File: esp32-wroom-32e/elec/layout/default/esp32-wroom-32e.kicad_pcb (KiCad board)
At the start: 2 copper layers, 40 x 40 mm, 16 parts

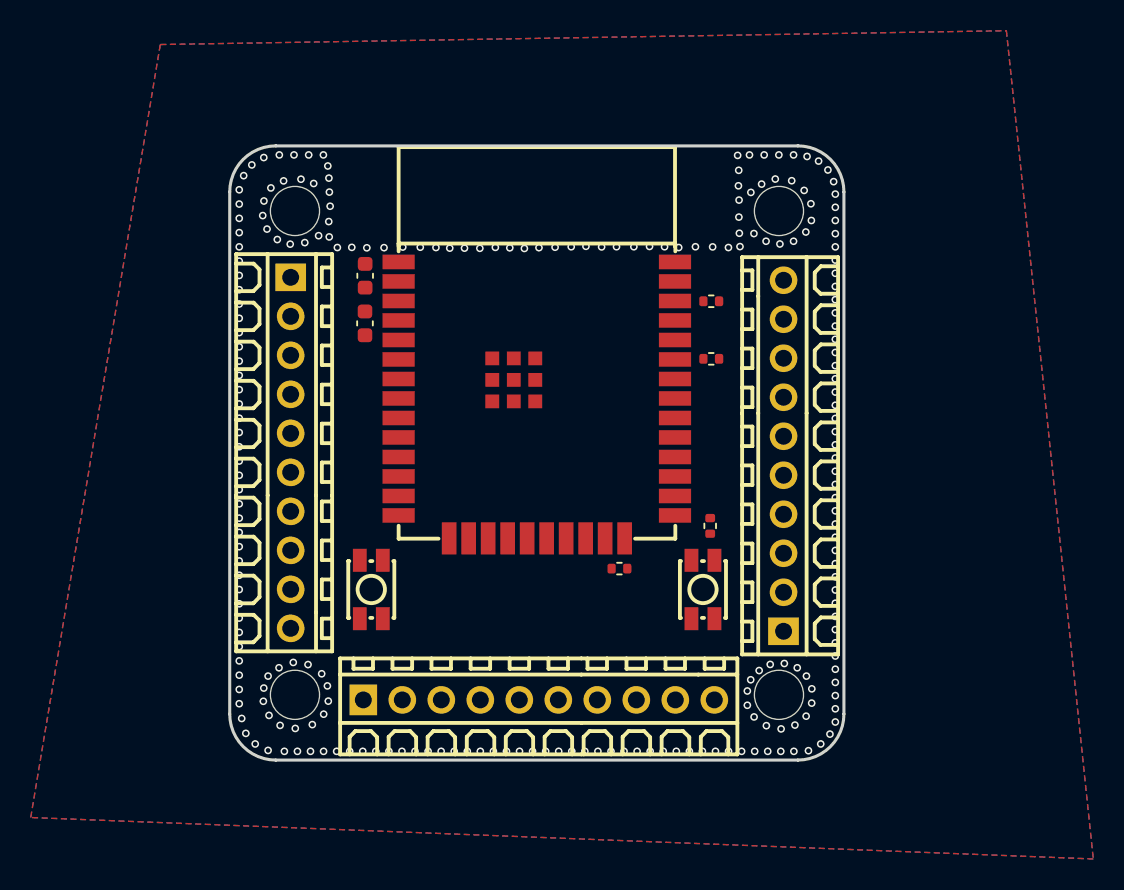
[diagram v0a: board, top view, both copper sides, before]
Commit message: updated footprints and pcb layout
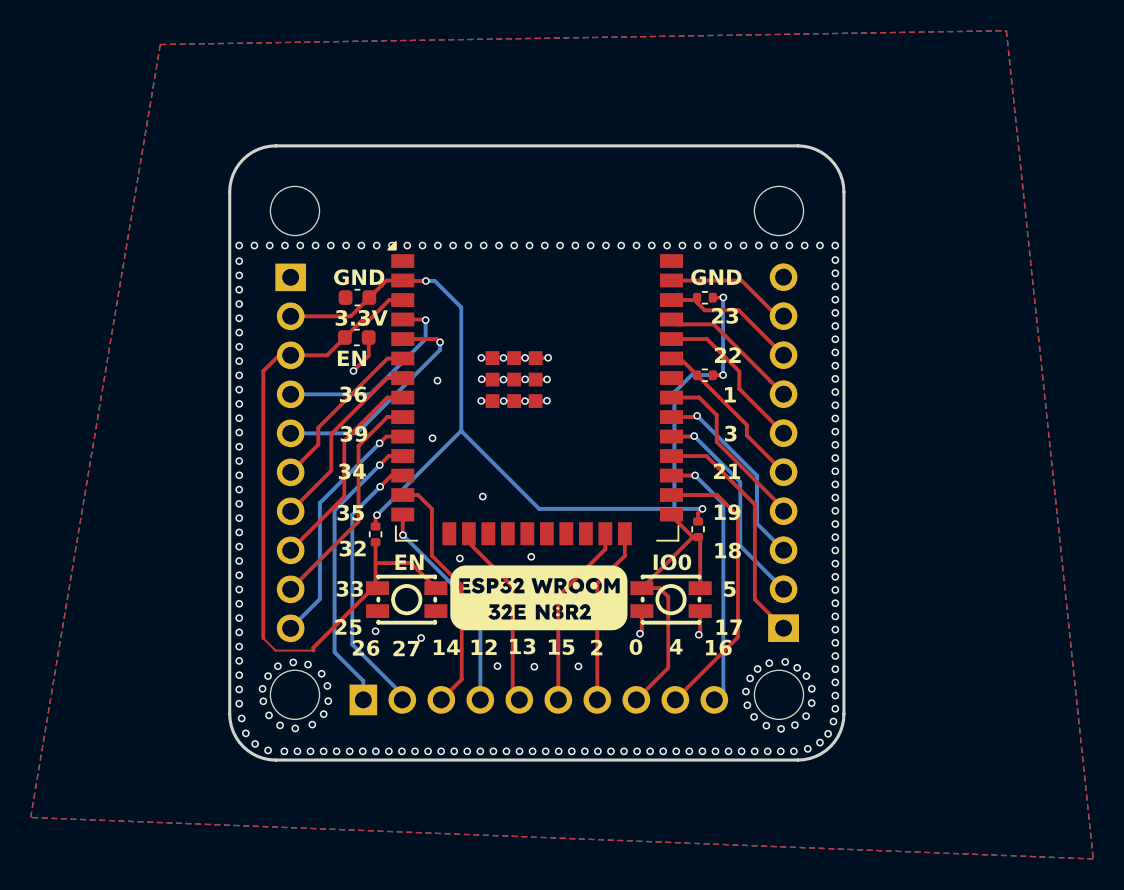
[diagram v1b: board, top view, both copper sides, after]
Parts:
- added REF**: OSHW-Logo2_7.3x6mm_SilkScreen, Symbol:OSHW-Logo2_7.3x6mm_SilkScreen, B.Cu at (124.2, 111.3)
- moved U3 19.5 mm to (141.6, 114.1), turned to 0 degrees
- moved U2 19.3 mm to (124.4, 114.1), turned to 0 degrees
- moved R3 16.0 mm to (122.3, 109.9), turned to 90 degrees
- moved U1 3.80 mm to (132.9, 97.3), turned to 0 degrees
- moved C1 1.51 mm to (121.2, 94.4), turned to 180 degrees
- moved R1 1.15 mm to (143.8, 99.5)
- moved C2 1.06 mm to (121.1, 97.0), turned to 0 degrees
- moved R4 0.82 mm to (143.3, 109.5), turned to 90 degrees
- moved R2 0.47 mm to (143.8, 94.5)
- moved U6 0.20 mm to (148.9, 104.5)
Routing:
- net vcc: track 0.00 -> 65.8 mm, vias 0 -> 5
- net reset: track 0.00 -> 45.6 mm
- net io0: track 0.00 -> 20.0 mm
- net sd: track 0.00 -> 19.0 mm, vias 0 -> 1
- net ic-sck-1: track 0.00 -> 18.6 mm
- net io27: track 0.00 -> 17.8 mm, vias 0 -> 1
- net io16: track 0.00 -> 17.2 mm, vias 0 -> 1
- net ic-sck: track 0.00 -> 16.1 mm, vias 0 -> 1
- net tms: track 0.00 -> 16.1 mm
- net io17: track 0.00 -> 15.6 mm
- net sensor_vn: track 0.00 -> 15.0 mm, vias 0 -> 1
- net io33: track 0.00 -> 14.8 mm
- net gnd: track 0.00 -> 14.4 mm, vias 231 -> 210
- net tdi: track 0.00 -> 14.2 mm, vias 0 -> 1
- net io5: track 0.00 -> 13.9 mm, vias 0 -> 1
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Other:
- board text added: "0"
- board text added: "1"
- board text added: "12"
- board text added: "13"
- board text added: "14"
- board text added: "15"
- board text added: "16"
- board text added: "17"
- board text added: "18"
- board text added: "19"
- board text added: "2"
- board text added: "21"
- board text added: "22"
- board text added: "23"
- board text added: "25"
- board text added: "26"
- board text added: "27"
- board text added: "3"
- board text added: "3.3V"
- board text added: "32"
- board text added: "33"
- board text added: "34"
- board text added: "35"
- board text added: "36"
- board text added: "39"
- board text added: "4"
- board text added: "5"
- board text added: "EN"
- board text added: "GND"
- board text added: "IO0"
- board text added: "Source files:"
- board text added: "bit.ly/3Xjrkh1"
- board text added: "designed by glowingkitty"
- board text added: "{{GITHASH}}"
